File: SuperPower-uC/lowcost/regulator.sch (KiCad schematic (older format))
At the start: 23 parts, among them Q5 AO3401A, Q6 AO3401A, Q7 2N7002, U10 FP6291LR, U11 ME6210A33P, U12 ME6210A33P

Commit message: swapped usb connector back to micro b, testpoints and other stuff
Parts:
- L1: footprint Inductor_SMD:L_0805_2012Metric_Pad1.15x1.40mm_HandSolder -> Inductor_SMD:L_Bourns_SRP7028A_7.3x6.6mm; LCSC C51725 -> C280586
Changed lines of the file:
@@
 F 0 "L1" H 5802 5046 50  0000 L CNN
 F 1 "3.3u" H 5802 4955 50  0000 L CNN
-F 2 "Inductor_SMD:L_0805_2012Metric_Pad1.15x1.40mm_HandSolder" H 5750 5000 50  0001 C CNN
-F 3 "~" H 5750 5000 50  0001 C CNN
-F 4 "C51725" H 5750 5000 50  0001 C CNN "LCSC"
+F 2 "Inductor_SMD:L_Bourns_SRP7028A_7.3x6.6mm" H 5750 5000 50  0001 C CNN
+F 3 "https://datasheet.lcsc.com/szlcsc/1912111437_Chilisin-Elec-MHCI06030-3R3M-R8A_C280586.pdf" H 5750 5000 50  0001 C CNN
+F 4 "C280586" H 5750 5000 50  0001 C CNN "LCSC"
 	1    5750 5000
 	0    -1   -1   0

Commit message: swapped pins for regulator and some more testpoints
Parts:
- added TP5, TP8: TestPoint, TestPoint:TestPoint_Pad_1.5x1.5mm, symbol Connector:TestPoint
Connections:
- wire segments 77 -> 81
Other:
- moved on the sheet: C11, C12, C13, C17, C18, D4, Q6, Q7, R13, R14, R15, R16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

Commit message: removed charge led and pcb stuff
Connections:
- wire segments 81 -> 83
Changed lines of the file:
@@
 	6100 5350 6650 5350
-Wire Wire Line
-	4900 5650 6200 5650
 Wire Wire Line
 	4900 5150 5400 5150
@@
 L power:GND #PWR0114
 U 1 1 5F827882
-P 6200 5650
-F 0 "#PWR0114" H 6200 5400 50  0001 C CNN
-F 1 "GND" H 6205 5477 50  0000 C CNN
-F 2 "" H 6200 5650 50  0001 C CNN
-F 3 "" H 6200 5650 50  0001 C CNN
-	1    6200 5650
+P 6050 5750
+F 0 "#PWR0114" H 6050 5500 50  0001 C CNN
+F 1 "GND" H 6055 5577 50  0000 C CNN
+F 2 "" H 6050 5750 50  0001 C CNN
+F 3 "" H 6050 5750 50  0001 C CNN
+	1    6050 5750
 	1    0    0    -1
 $EndComp
@@
 	1    0    0    -1
 $EndComp
+Wire Wire Line
+	4900 5650 6050 5650
+Wire Wire Line
+	6050 5650 6050 5750
+Connection ~ 6050 5650
+Wire Wire Line
+	6050 5650 6200 5650
 $EndSCHEMATC

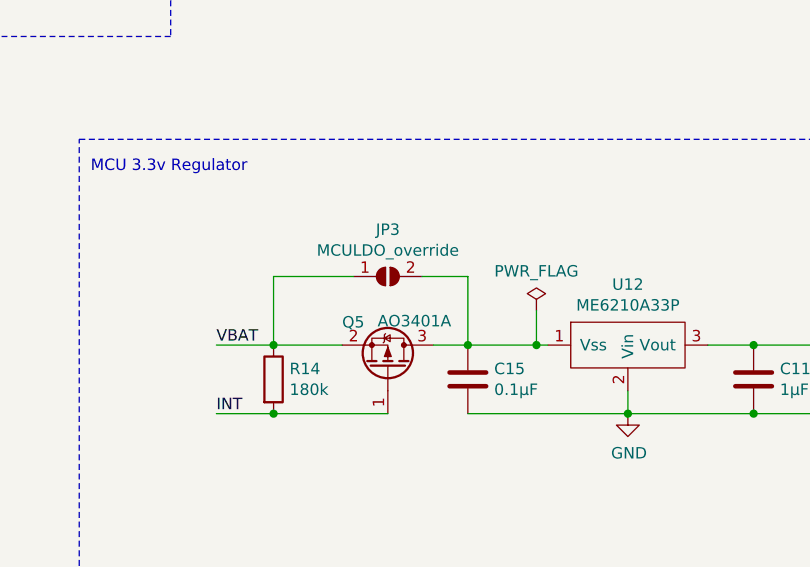
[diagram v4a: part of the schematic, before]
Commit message: finished pcb layout for review
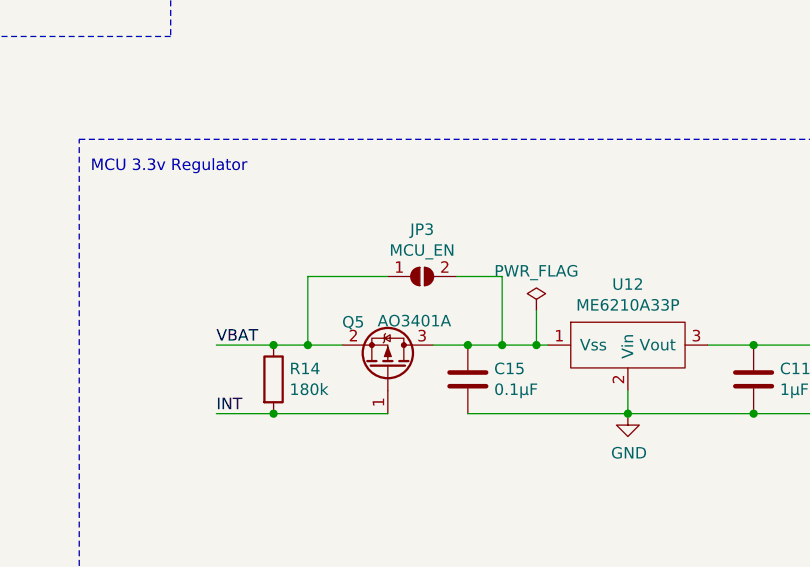
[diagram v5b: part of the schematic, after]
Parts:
- D4: footprint Diode_SMD:D_SMA_Handsoldering -> Diode_SMD:D_SOD-123; LCSC C8678 -> C8598
- JP3: value MCULDO_override -> MCU_EN
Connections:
- wire segments 83 -> 85
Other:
- moved on the sheet: JP3
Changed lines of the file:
@@
 $EndComp
 Wire Wire Line
-	2550 3200 2250 3200
+	2550 3200 2400 3200
 $Comp
 L Transistor_FET:2N7002 Q7
@@
 Connection ~ 3100 3200
 Wire Wire Line
-	3100 3200 3400 3200
+	3100 3200 3250 3200
 Wire Wire Line
 	3100 3500 3800 3500
@@
 Connection ~ 2250 3200
 Wire Wire Line
-	2900 2900 3100 2900
+	3050 2900 3250 2900
 $Comp
 L Jumper:SolderJumper_2_Open JP3
 U 1 1 5F81FE3B
-P 2750 2900
-F 0 "JP3" H 2750 3105 50  0000 C CNN
-F 1 "MCULDO_override" H 2750 3014 50  0000 C CNN
-F 2 "Jumper:SolderJumper-2_P1.3mm_Open_Pad1.0x1.5mm" H 2750 2900 50  0001 C CNN
-F 3 "~" H 2750 2900 50  0001 C CNN
-	1    2750 2900
-	1    0    0    -1
-$EndComp
-Wire Wire Line
-	2250 2900 2250 3200
-Wire Wire Line
-	3100 2900 3100 3200
-Wire Wire Line
-	2250 2900 2600 2900
+P 2900 2900
+F 0 "JP3" H 2900 3105 50  0000 C CNN
+F 1 "MCU_EN" H 2900 3014 50  0000 C CNN
+F 2 "Jumper:SolderJumper-2_P1.3mm_Open_Pad1.0x1.5mm" H 2900 2900 50  0001 C CNN
+F 3 "~" H 2900 2900 50  0001 C CNN
+	1    2900 2900
+	1    0    0    -1
+$EndComp
+Wire Wire Line
+	2400 2900 2400 3200
+Wire Wire Line
+	3250 2900 3250 3200
+Wire Wire Line
+	2400 2900 2750 2900
 $Comp
 L Device:C C16
@@
 F 0 "D4" H 6400 4783 50  0000 C CNN
 F 1 "D_Schottky" H 6400 4874 50  0000 C CNN
-F 2 "Diode_SMD:D_SMA_Handsoldering" H 6400 5000 50  0001 C CNN
-F 3 "https://datasheet.lcsc.com/szlcsc/1903051003_MDD-Jiangsu-Yutai-Elec-SS34_C8678.pdf" H 6400 5000 50  0001 C CNN
-F 4 "C8678" H 6400 5000 50  0001 C CNN "LCSC"
+F 2 "Diode_SMD:D_SOD-123" H 6400 5000 50  0001 C CNN
+F 3 "https://datasheet.lcsc.com/szlcsc/Changjiang-Electronics-Tech-CJ-B5819W_C8598.pdf" H 6400 5000 50  0001 C CNN
+F 4 " C8598" H 6400 5000 50  0001 C CNN "LCSC"
 	1    6400 5000
 	-1   0    0    1
@@
 Wire Wire Line
 	6050 5650 6200 5650
+Connection ~ 2400 3200
+Wire Wire Line
+	2400 3200 2250 3200
+Connection ~ 3250 3200
+Wire Wire Line
+	3250 3200 3400 3200
 $EndSCHEMATC

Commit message: swapped inductor for 5v booster
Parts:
- L1: LCSC C280586 -> C207841
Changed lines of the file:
@@
 F 1 "3.3u" H 5802 4955 50  0000 L CNN
 F 2 "Inductor_SMD:L_Bourns_SRP7028A_7.3x6.6mm" H 5750 5000 50  0001 C CNN
-F 3 "https://datasheet.lcsc.com/szlcsc/1912111437_Chilisin-Elec-MHCI06030-3R3M-R8A_C280586.pdf" H 5750 5000 50  0001 C CNN
-F 4 "C280586" H 5750 5000 50  0001 C CNN "LCSC"
+F 3 "https://datasheet.lcsc.com/szlcsc/1811091611_Sunltech-Tech-SLO0630H6R8MTT_C207841.pdf" H 5750 5000 50  0001 C CNN
+F 4 "C207841" H 5750 5000 50  0001 C CNN "LCSC"
 	1    5750 5000
 	0    -1   -1   0

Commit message: added proper high side cutoff for 5v regulator
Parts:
- added Q8: 2N7002, Package_TO_SOT_SMD:SOT-23, symbol Transistor_FET:2N7002
- added Q9: AO3401A, Package_TO_SOT_SMD:SOT-23_Handsoldering, symbol Transistor_FET:AO3401A
- added R19: 180k, Resistor_SMD:R_0603_1608Metric_Pad1.05x0.95mm_HandSolder, symbol Device:R
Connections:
- wire segments 85 -> 92
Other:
- moved on the sheet: C12, C13, C17, D4, L1, R15, R16, R17, U10

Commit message: increased pullup values and added caps
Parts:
- added C23: 1µF, Capacitor_SMD:C_0603_1608Metric_Pad1.05x0.95mm_HandSolder, symbol Device:C
- added C24, C25: 0.1µF, Capacitor_SMD:C_0603_1608Metric_Pad1.05x0.95mm_HandSolder, symbol Device:C
- R13, R14, R19: value 180k -> 1M; LCSC C22827 -> C22935
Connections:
- wire segments 92 -> 110
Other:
- moved on the sheet: C11, C12, C13, C15, C17, C18, D4, JP3, L1, Q5, Q6, Q7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
